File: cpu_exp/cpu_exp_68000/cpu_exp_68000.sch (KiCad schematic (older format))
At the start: 15 parts

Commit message: Updates from SVN to rev3.03
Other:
- note added: "TODO: pull up resistors on RESET, HALT\nRotate pin labels to be rotationally symetrical"
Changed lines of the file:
@@
 	1    0    0    -1
 $EndComp
+Text Notes 2450 3050 0    50   ~ 0
+TODO: pull up resistors on RESET, HALT\nRotate pin labels to be rotationally symetrical
 $EndSCHEMATC

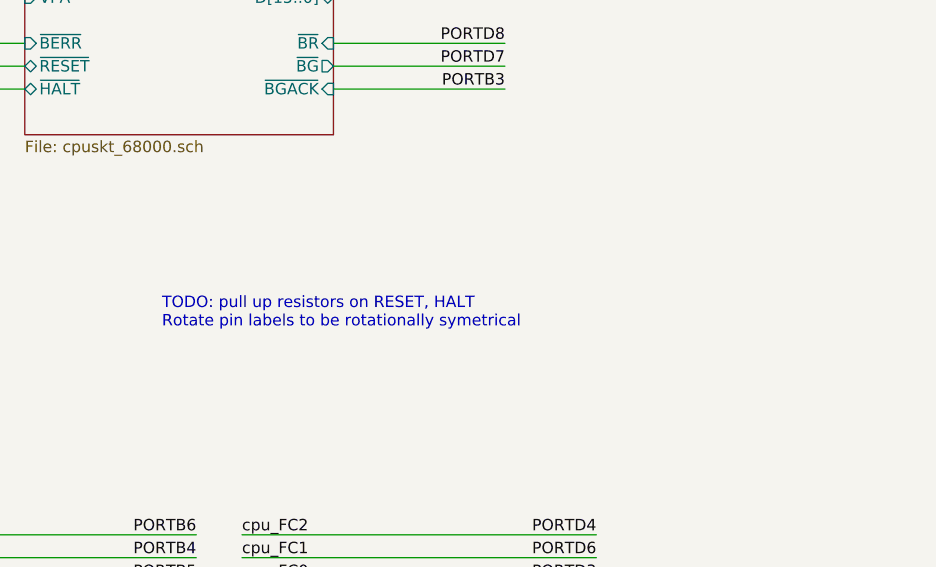
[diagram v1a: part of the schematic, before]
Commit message: Add fixit notes to 68000 cpu board for next revision
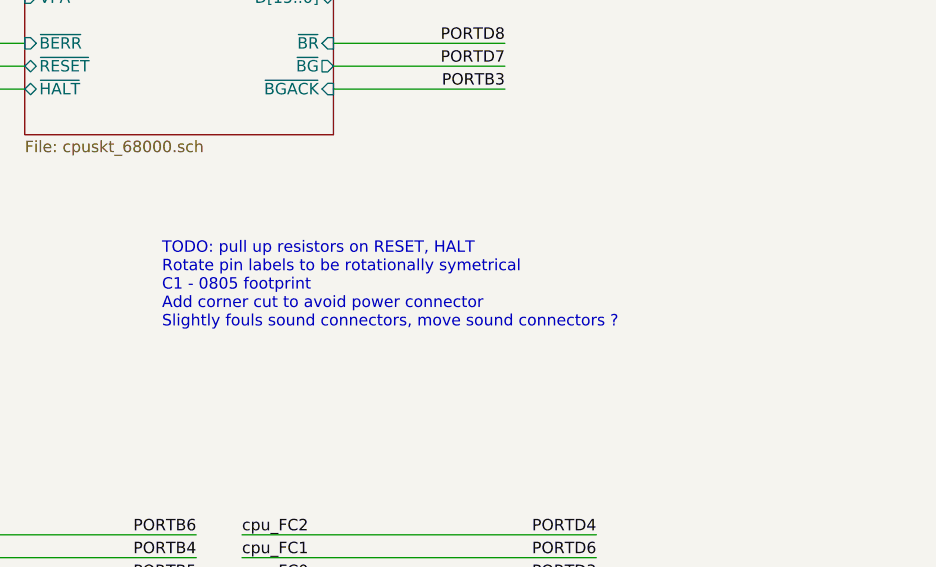
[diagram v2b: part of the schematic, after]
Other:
- note added: "TODO: pull up resistors on RESET, HALT\nRotate pin labels to be rotationally symetrical\nC1 - 0805 footprint\nAdd corner cut to avoid power connector\nSlightly fouls sound connectors, move sound connectors ?"
- note removed: "TODO: pull up resistors on RESET, HALT\nRotate pin labels to be rotationally symetrical"
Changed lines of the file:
@@
 $EndComp
 Text Notes 2450 3050 0    50   ~ 0
-TODO: pull up resistors on RESET, HALT\nRotate pin labels to be rotationally symetrical
+TODO: pull up resistors on RESET, HALT\nRotate pin labels to be rotationally symetrical\nC1 - 0805 footprint\nAdd corner cut to avoid power connector\nSlightly fouls sound connectors, move sound connectors ?
 $EndSCHEMATC
